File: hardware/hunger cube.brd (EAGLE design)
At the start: 84.1 x 63.5 mm, 37 parts, among them IC1 AVR-MEGA8-PPTH, IC2 LDO 5v, Q1 16Mhz, T1 PT204, T2 PT204

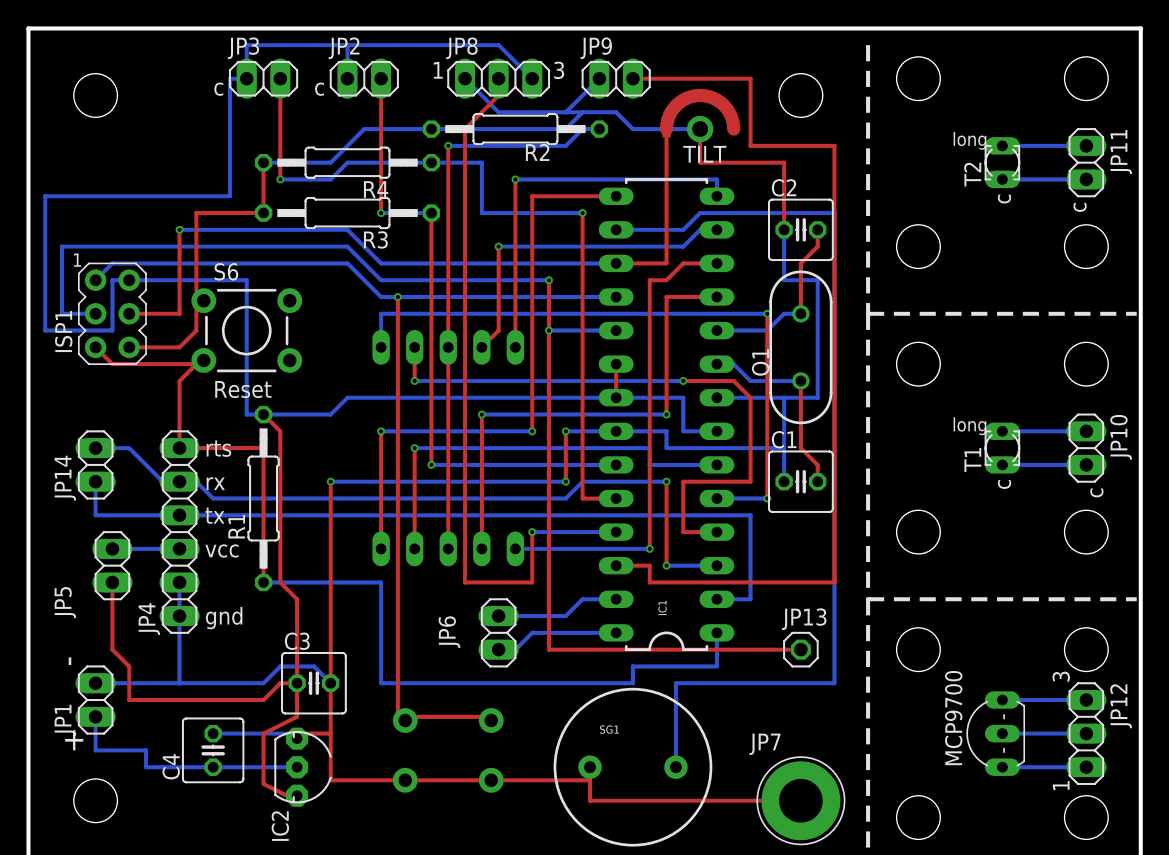
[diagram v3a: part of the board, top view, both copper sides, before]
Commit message: 
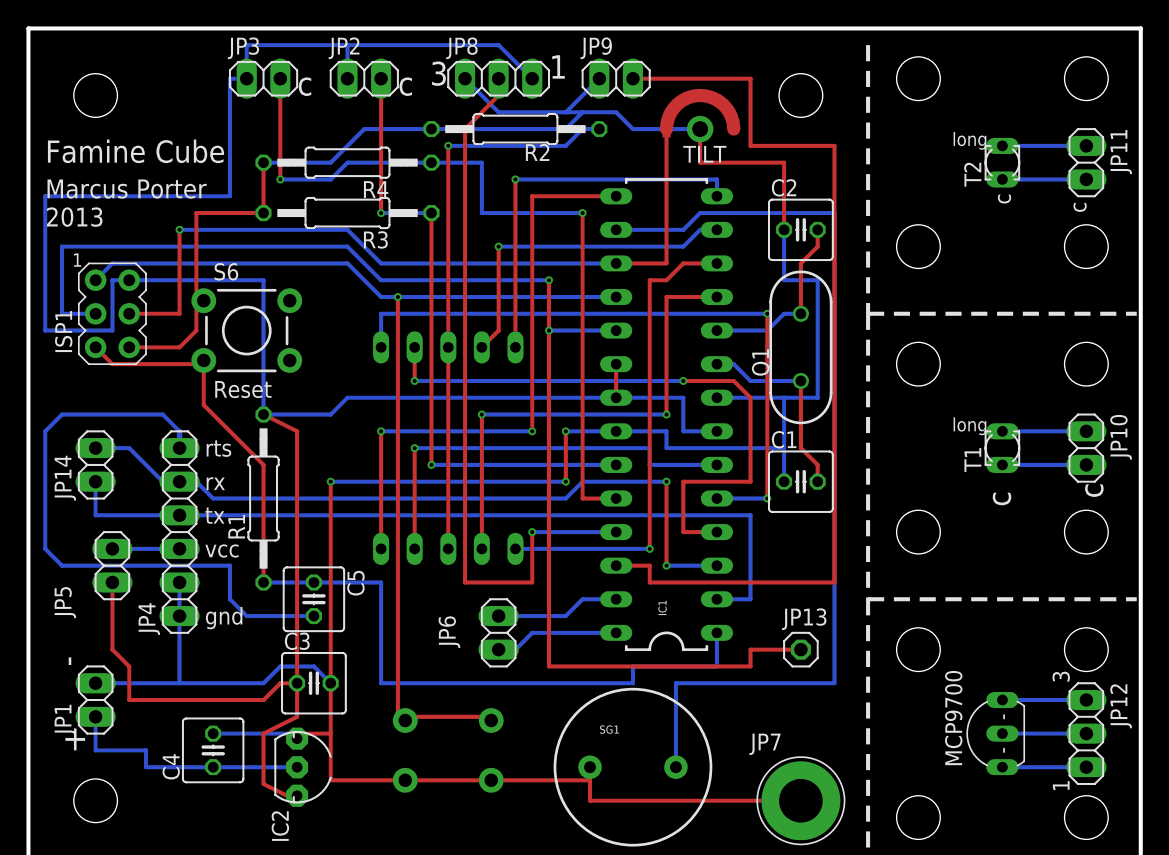
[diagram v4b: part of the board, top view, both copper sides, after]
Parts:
- added C5: .1 uf, resistor:C025-050X050
- DIS1: value HD-H101 -> display
- T1: value PT204 -> light
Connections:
- net N$12 renamed DSP-GND
- new net N$1: C5.2, JP4.6
- net RST: now also C5.1; no longer JP4.6
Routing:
- net N$1: track 0.00 -> 45.3 mm
- net RST: track 78.5 -> 73.8 mm
- net D13-SCK-SCREW: track 97.6 -> 100.1 mm
- net +5V: track 188.8 -> 189.3 mm
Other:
- board text added: "Famine Cube"
- board text added: "Marcus Porter 2013"
- board text added: "dp"

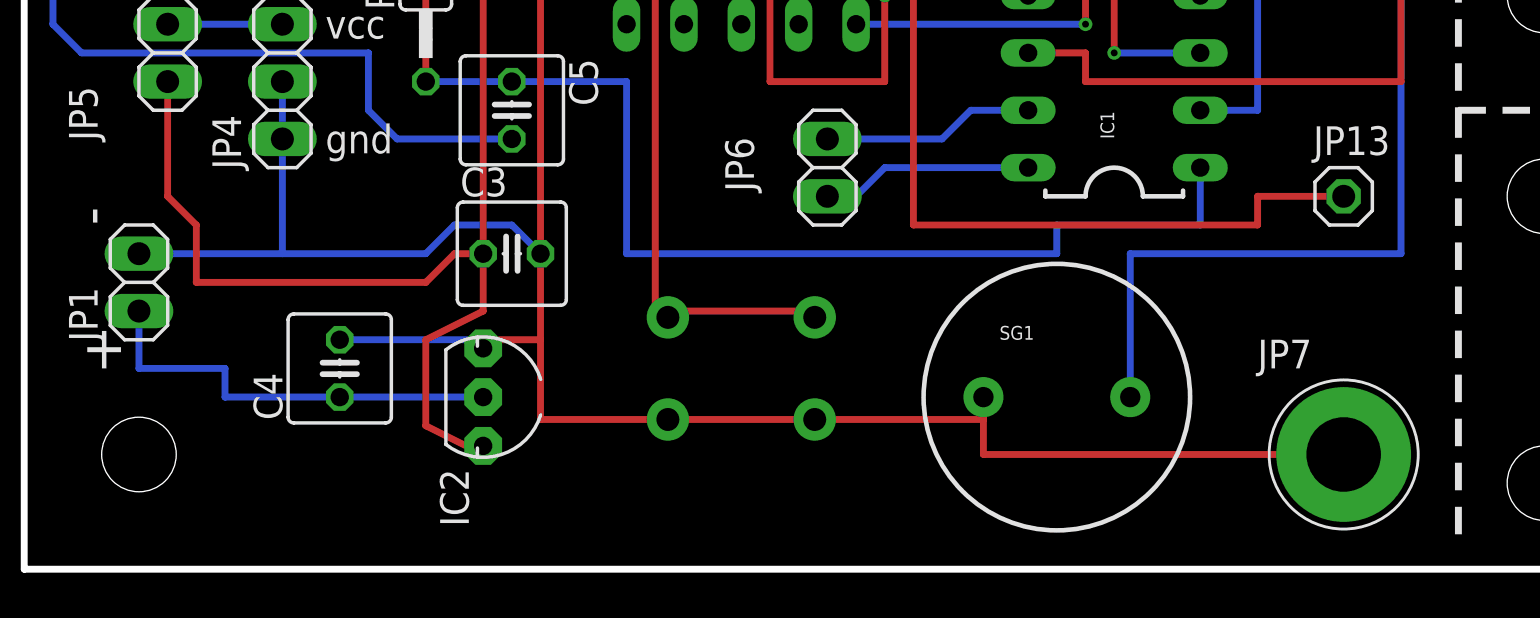
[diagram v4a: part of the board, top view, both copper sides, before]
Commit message: 
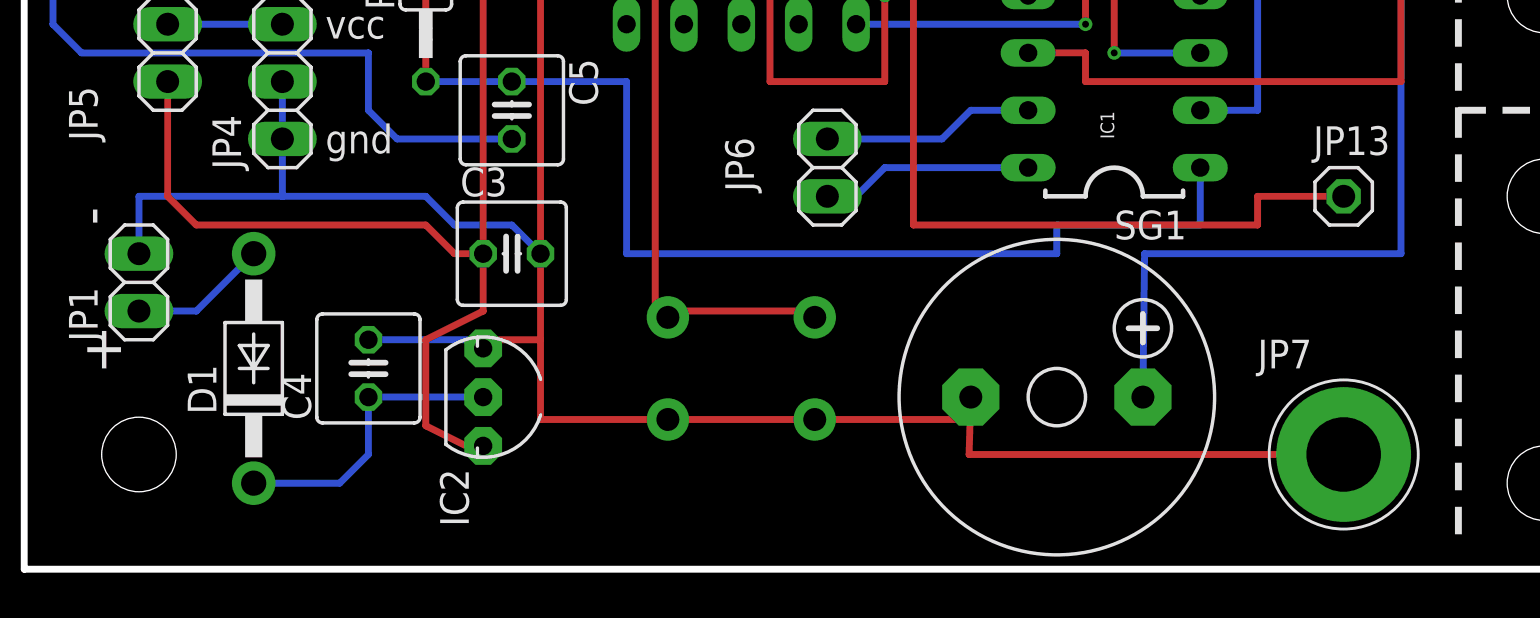
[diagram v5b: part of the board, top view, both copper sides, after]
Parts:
- added D1: (no value), adafruit:DO41-10
- SG1: value BUZZERPTH -> F/CM12P; device SparkFun:BUZZER-12MM -> buzzer:F/CM12P
- moved C4 1.27 mm to (15.2, 8.89)
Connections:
- new net N$2: D1.A, JP1.1
- net VCC: now also D1.C; no longer JP1.1
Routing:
- net N$2: track 0.00 -> 6.13 mm
- net VCC: track 19.0 -> 13.2 mm
- net +5V: track 189.3 -> 186.8 mm
- net GND: track 253.0 -> 251.7 mm
- net D10-BUZZER: track 70.9 -> 70.3 mm
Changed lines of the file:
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@@
 <attribute name="VALUE" x="24.384" y="13.97" size="1.27" layer="27" ratio="10"/>
 </element>
-<element name="C4" library="resistor" package="C025-050X050" value="1 uf" x="13.97" y="8.89" smashed="yes" rot="R90">
-<attribute name="NAME" x="11.43" y="6.604" size="1.27" layer="25" ratio="10" rot="R90"/>
-<attribute name="VALUE" x="13.97" y="11.684" size="1.27" layer="27" ratio="10" rot="R90"/>
+<element name="C4" library="resistor" package="C025-050X050" value="1 uf" x="15.24" y="8.89" smashed="yes" rot="R90">
+<attribute name="NAME" x="12.7" y="6.604" size="1.27" layer="25" ratio="10" rot="R90"/>
+<attribute name="VALUE" x="15.24" y="11.684" size="1.27" layer="27" ratio="10" rot="R90"/>
 </element>
 <element name="R2" library="resistor" package="0207/12" value="100" x="36.83" y="55.88" smashed="yes">
@@
 <attribute name="NAME" x="49.53" y="53.34" size="1.27" layer="21"/>
 </element>
-<element name="SG1" library="SparkFun" package="BUZZER-12MM" value="BUZZERPTH" x="45.72" y="7.62"/>
+<element name="SG1" library="buzzer" package="F/CM12P" value="F/CM12P" x="45.72" y="7.62">
+<attribute name="OC_NEWARK" value="unknown" x="45.72" y="7.62" size="1.778" layer="27" display="off"/>
+<attribute name="MPN" value="" x="45.72" y="7.62" size="1.778" layer="27" display="off"/>
+<attribute name="MF" value="" x="45.72" y="7.62" size="1.778" layer="27" display="off"/>
+<attribute name="OC_FARNELL" value="unknown" x="45.72" y="7.62" size="1.778" layer="27" display="off"/>
+</element>
 <element name="JP6" library="pinhead" package="1X02" value="A5 A4" x="35.56" y="17.78" smashed="yes" rot="R270">
 <attribute name="NAME" x="31.0388" y="19.1262" size="1.27" layer="25" ratio="10" rot="R270"/>
@@
 <element name="JP14" library="pinhead" package="1X02" value="D0 D1" x="5.08" y="30.48" rot="R90"/>
 <element name="C5" library="resistor" package="C025-050X050" value=".1 uf" x="21.59" y="20.32" rot="R270"/>
+<element name="D1" library="adafruit" package="DO41-10" value="" x="10.16" y="8.89" rot="R90"/>
 </elements>
 <signals>
@@
 <wire x1="25.4" y1="55.88" x2="22.86" y2="53.34" width="0.3048" layer="16"/>
 <wire x1="30.48" y1="55.88" x2="25.4" y2="55.88" width="0.3048" layer="16"/>
-<wire x1="13.97" y1="10.16" x2="20.32" y2="10.16" width="0.3048" layer="16"/>
+<wire x1="15.24" y1="10.16" x2="20.32" y2="10.16" width="0.3048" layer="16"/>
 <wire x1="20.32" y1="10.16" x2="20.32" y2="9.779" width="0.3048" layer="16"/>
 <wire x1="11.43" y1="19.05" x2="11.43" y2="21.59" width="0.3048" layer="16"/>
 <wire x1="21.59" y1="15.24" x2="22.86" y2="13.97" width="0.3048" layer="16"/>
 <wire x1="19.05" y1="15.24" x2="21.59" y2="15.24" width="0.3048" layer="16"/>
-<wire x1="17.78" y1="13.97" x2="19.05" y2="15.24" width="0.3048" layer="16"/>
-<wire x1="5.08" y1="13.97" x2="11.43" y2="13.97" width="0.3048" layer="16"/>
-<wire x1="11.43" y1="13.97" x2="17.78" y2="13.97" width="0.3048" layer="16"/>
-<wire x1="11.43" y1="13.97" x2="11.43" y2="19.05" width="0.3048" layer="16"/>
+<wire x1="17.78" y1="16.51" x2="19.05" y2="15.24" width="0.3048" layer="16"/>
+<wire x1="5.08" y1="13.97" x2="5.08" y2="16.51" width="0.3048" layer="16"/>
+<wire x1="5.08" y1="16.51" x2="11.43" y2="16.51" width="0.3048" layer="16"/>
+<wire x1="11.43" y1="16.51" x2="17.78" y2="16.51" width="0.3048" layer="16"/>
+<wire x1="11.43" y1="16.51" x2="11.43" y2="19.05" width="0.3048" layer="16"/>
 <wire x1="22.86" y1="10.16" x2="20.32" y2="10.16" width="0.3048" layer="1"/>
 <wire x1="22.86" y1="13.97" x2="22.86" y2="10.16" width="0.3048" layer="1"/>
@@
 <wire x1="22.86" y1="6.6294" x2="28.4988" y2="6.6294" width="0.3048" layer="1"/>
 <wire x1="28.4988" y1="6.6294" x2="35.0012" y2="6.6294" width="0.3048" layer="1"/>
-<wire x1="35.0012" y1="6.6294" x2="42.47" y2="6.6294" width="0.3048" layer="1"/>
-<wire x1="42.47" y1="6.6294" x2="42.47" y2="7.62" width="0.3048" layer="1"/>
-<wire x1="42.47" y1="7.62" x2="42.47" y2="5.08" width="0.3048" layer="1"/>
-<wire x1="42.47" y1="5.08" x2="58.42" y2="5.08" width="0.3048" layer="1"/>
+<wire x1="35.0012" y1="6.6294" x2="41.835" y2="6.6294" width="0.3048" layer="1"/>
+<wire x1="41.835" y1="6.6294" x2="41.91" y2="7.62" width="0.3048" layer="1"/>
+<wire x1="41.91" y1="7.62" x2="41.835" y2="5.08" width="0.3048" layer="1"/>
+<wire x1="41.835" y1="5.08" x2="58.42" y2="5.08" width="0.3048" layer="1"/>
 <wire x1="50.8" y1="55.88" x2="50.8" y2="53.34" width="0.3048" layer="1"/>
 <wire x1="50.8" y1="53.34" x2="57.15" y2="53.34" width="0.3048" layer="1"/>
@@
 <contactref element="IC2" pad="2"/>
 <contactref element="C4" pad="1"/>
-<contactref element="JP1" pad="1"/>
-<wire x1="13.97" y1="7.62" x2="20.32" y2="7.62" width="0.3048" layer="16"/>
-<wire x1="5.08" y1="11.43" x2="5.08" y2="8.89" width="0.3048" layer="16"/>
-<wire x1="5.08" y1="8.89" x2="8.89" y2="8.89" width="0.3048" layer="16"/>
-<wire x1="8.89" y1="8.89" x2="8.89" y2="7.62" width="0.3048" layer="16"/>
-<wire x1="8.89" y1="7.62" x2="13.97" y2="7.62" width="0.3048" layer="16"/>
+<wire x1="15.24" y1="7.62" x2="20.32" y2="7.62" width="0.3048" layer="16"/>
+<contactref element="D1" pad="C"/>
+<wire x1="10.16" y1="3.81" x2="13.97" y2="3.81" width="0.3048" layer="16"/>
+<wire x1="13.97" y1="3.81" x2="15.24" y2="5.08" width="0.3048" layer="16"/>
+<wire x1="15.24" y1="5.08" x2="15.24" y2="7.62" width="0.3048" layer="16"/>
 </signal>
 <signal name="+5V">
@@
 <wire x1="6.35" y1="16.51" x2="6.35" y2="21.59" width="0.3048" layer="1"/>
 <wire x1="7.62" y1="15.24" x2="6.35" y2="16.51" width="0.3048" layer="1"/>
-<wire x1="7.62" y1="12.7" x2="7.62" y2="15.24" width="0.3048" layer="1"/>
-<wire x1="17.78" y1="12.7" x2="7.62" y2="12.7" width="0.3048" layer="1"/>
-<wire x1="19.05" y1="13.97" x2="17.78" y2="12.7" width="0.3048" layer="1"/>
+<wire x1="17.78" y1="15.24" x2="7.62" y2="15.24" width="0.3048" layer="1"/>
+<wire x1="19.05" y1="13.97" x2="17.78" y2="15.24" width="0.3048" layer="1"/>
 <wire x1="20.32" y1="13.97" x2="19.05" y2="13.97" width="0.3048" layer="1"/>
 <wire x1="24.13" y1="35.56" x2="44.45" y2="35.56" width="0.3048" layer="16"/>
@@
 <wire x1="60.96" y1="49.53" x2="50.8" y2="49.53" width="0.3048" layer="16"/>
 <wire x1="60.96" y1="13.97" x2="60.96" y2="49.53" width="0.3048" layer="16"/>
-<wire x1="48.97" y1="13.97" x2="60.96" y2="13.97" width="0.3048" layer="16"/>
-<wire x1="48.97" y1="13.97" x2="48.97" y2="7.62" width="0.3048" layer="16"/>
+<wire x1="49.605" y1="13.97" x2="60.96" y2="13.97" width="0.3048" layer="16"/>
+<wire x1="49.605" y1="13.97" x2="49.53" y2="7.62" width="0.3048" layer="16"/>
 </signal>
 <signal name="A4">
@@
 <wire x1="11.43" y1="33.02" x2="11.43" y2="31.75" width="0.4064" layer="16"/>
 </signal>
+<signal name="N$2">
+<contactref element="JP1" pad="1"/>
+<contactref element="D1" pad="A"/>
+<wire x1="5.08" y1="11.43" x2="7.62" y2="11.43" width="0.3048" layer="16"/>
+<wire x1="7.62" y1="11.43" x2="10.16" y2="13.97" width="0.3048" layer="16"/>
+</signal>
 </signals>

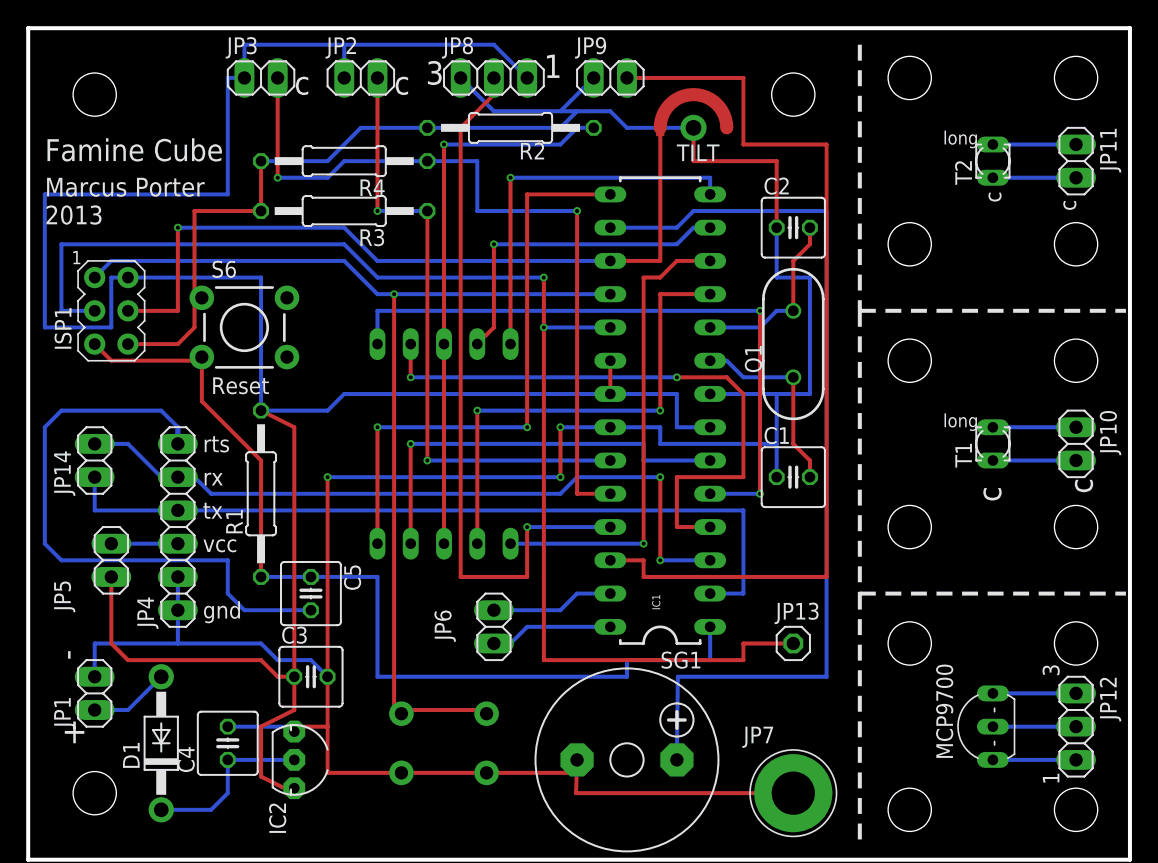
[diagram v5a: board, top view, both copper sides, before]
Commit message: 
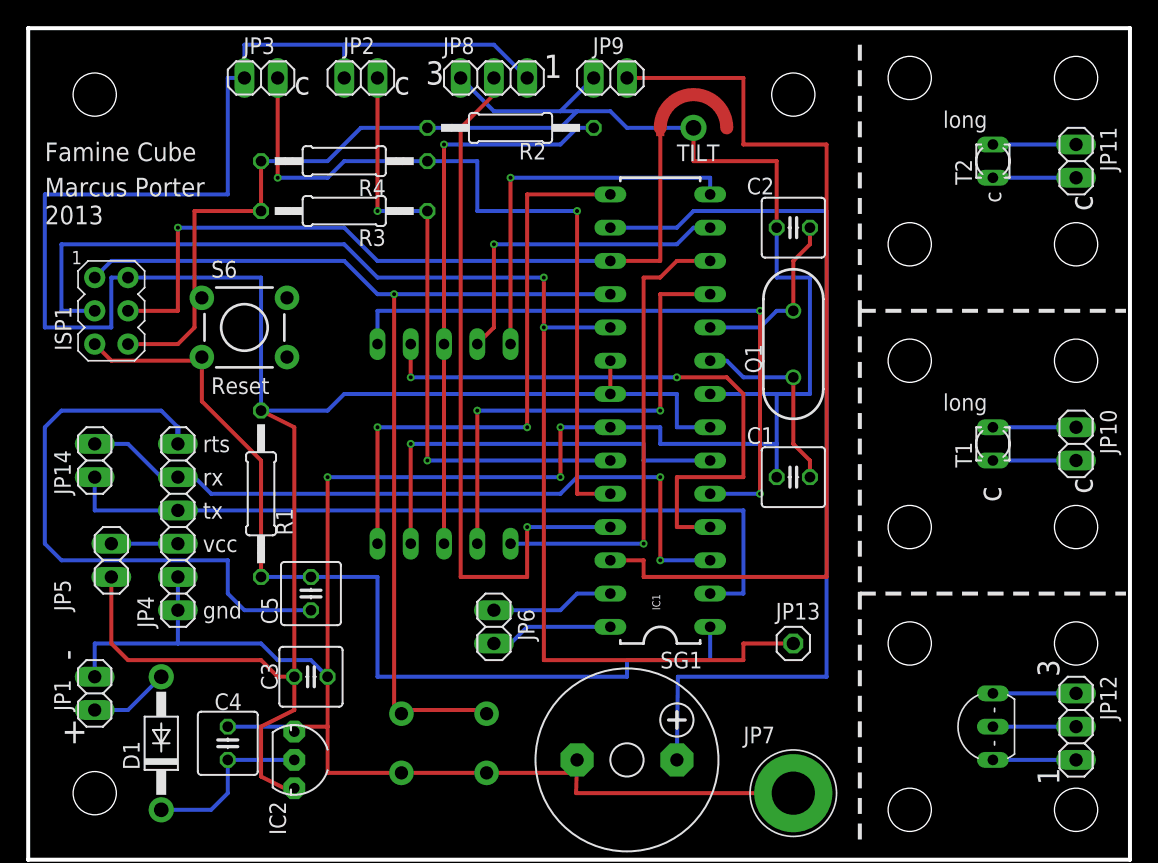
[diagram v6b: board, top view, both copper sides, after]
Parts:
- C3, C4: value 1 uf -> 1uf
- C5: value .1 uf -> .1uf
- JP10: value R Light 1 -> RLight1
- JP11: value R light 2 -> Rlight2
- JP12: value R temp -> Rtemp
- JP3: value Light 2 -> Light2
- R3, R4: value (none) -> 10K
- T2: value PT204 -> light
- TEMPERATURE: value temp -> Temperature
- renumbered MCP9700 to TEMPERATURE
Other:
- board text added: "DP"
